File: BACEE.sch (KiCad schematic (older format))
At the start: 0 parts

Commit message: Create new shild sheet, added roject symbols
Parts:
- added BT?: Battery, symbol Device:Battery
- added C? (x2): C, symbol Device:C
- added C?: CP, symbol Device:CP
- added D?: LED, symbol Device:LED
- added R? (x2): R, symbol Device:R
- added U?: 24LC1025, symbol Memory_EEPROM:24LC1025
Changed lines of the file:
@@
 $Descr A4 11693 8268
 encoding utf-8
-Sheet 1 1
+Sheet 1 2
 Title "Battery Powered Arduino with clock and extended eeprom"
 Date "2020-05-17"
@@
 Comment4 ""
 $EndDescr
+$Comp
+L Device:Battery BT?
+U 1 1 5EC0DCA7
+P 5050 3050
+F 0 "BT?" H 5158 3096 50  0000 L CNN
+F 1 "Battery" H 5158 3005 50  0000 L CNN
+F 2 "" V 5050 3110 50  0001 C CNN
+F 3 "~" V 5050 3110 50  0001 C CNN
+	1    5050 3050
+	1    0    0    -1
+$EndComp
+$Comp
+L Device:C C?
+U 1 1 5EC0FEED
+P 5600 3000
+F 0 "C?" H 5715 3046 50  0000 L CNN
+F 1 "C" H 5715 2955 50  0000 L CNN
+F 2 "" H 5638 2850 50  0001 C CNN
+F 3 "~" H 5600 3000 50  0001 C CNN
+	1    5600 3000
+	1    0    0    -1
+$EndComp
+$Comp
+L Device:C C?
+U 1 1 5EC1064E
+P 5600 3500
+F 0 "C?" H 5715 3546 50  0000 L CNN
+F 1 "C" H 5715 3455 50  0000 L CNN
+F 2 "" H 5638 3350 50  0001 C CNN
+F 3 "~" H 5600 3500 50  0001 C CNN
+	1    5600 3500
+	1    0    0    -1
+$EndComp
+$Comp
+L Device:CP C?
+U 1 1 5EC10D42
+P 5600 4000
+F 0 "C?" H 5718 4046 50  0000 L CNN
+F 1 "CP" H 5718 3955 50  0000 L CNN
+F 2 "" H 5638 3850 50  0001 C CNN
+F 3 "~" H 5600 4000 50  0001 C CNN
+	1    5600 4000
+	1    0    0    -1
+$EndComp
+$Comp
+L Device:LED D?
+U 1 1 5EC11BF2
+P 5050 3750
+F 0 "D?" H 5043 3966 50  0000 C CNN
+F 1 "LED" H 5043 3875 50  0000 C CNN
+F 2 "" H 5050 3750 50  0001 C CNN
+F 3 "~" H 5050 3750 50  0001 C CNN
+	1    5050 3750
+	1    0    0    -1
+$EndComp
+$Comp
+L Device:R R?
+U 1 1 5EC1258B
+P 6300 3100
+F 0 "R?" H 6370 3146 50  0000 L CNN
+F 1 "R" H 6370 3055 50  0000 L CNN
+F 2 "" V 6230 3100 50  0001 C CNN
+F 3 "~" H 6300 3100 50  0001 C CNN
+	1    6300 3100
+	1    0    0    -1
+$EndComp
+$Comp
+L Device:R R?
+U 1 1 5EC1288A
+P 6300 3600
+F 0 "R?" H 6370 3646 50  0000 L CNN
+F 1 "R" H 6370 3555 50  0000 L CNN
+F 2 "" V 6230 3600 50  0001 C CNN
+F 3 "~" H 6300 3600 50  0001 C CNN
+	1    6300 3600
+	1    0    0    -1
+$EndComp
+$Comp
+L Memory_EEPROM:24LC1025 U?
+U 1 1 5EC12FEA
+P 7150 3050
+F 0 "U?" H 7150 3531 50  0000 C CNN
+F 1 "24LC1025" H 7150 3440 50  0000 C CNN
+F 2 "" H 7150 3050 50  0001 C CNN
+F 3 "http://ww1.microchip.com/downloads/en/DeviceDoc/21941B.pdf" H 7150 3050 50  0001 C CNN
+	1    7150 3050
+	1    0    0    -1
+$EndComp
+$Sheet
+S 6950 3850 1150 1600
+U 5EC178C4
+F0 "Connectors" 50
+F1 "Connectors.sch" 50
+$EndSheet
 $EndSCHEMATC

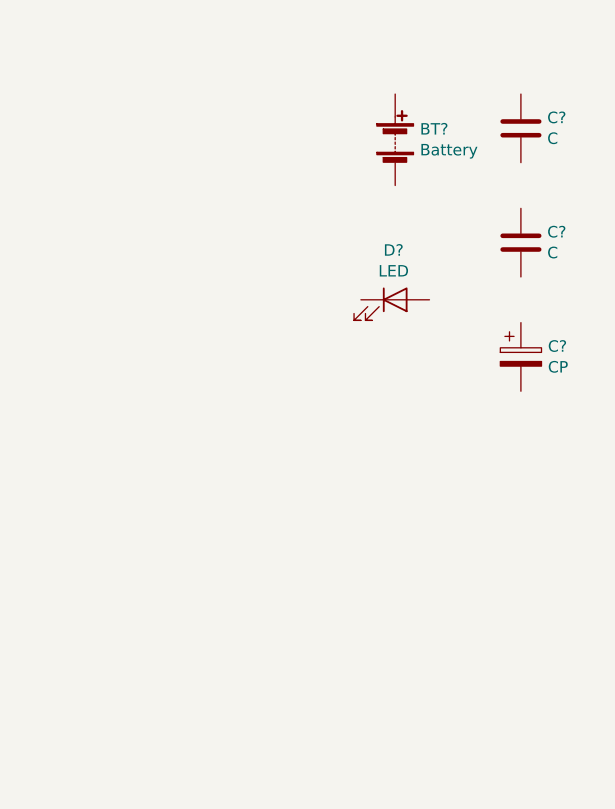
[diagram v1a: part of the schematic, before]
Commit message: Added symbol for Atmega328p-au
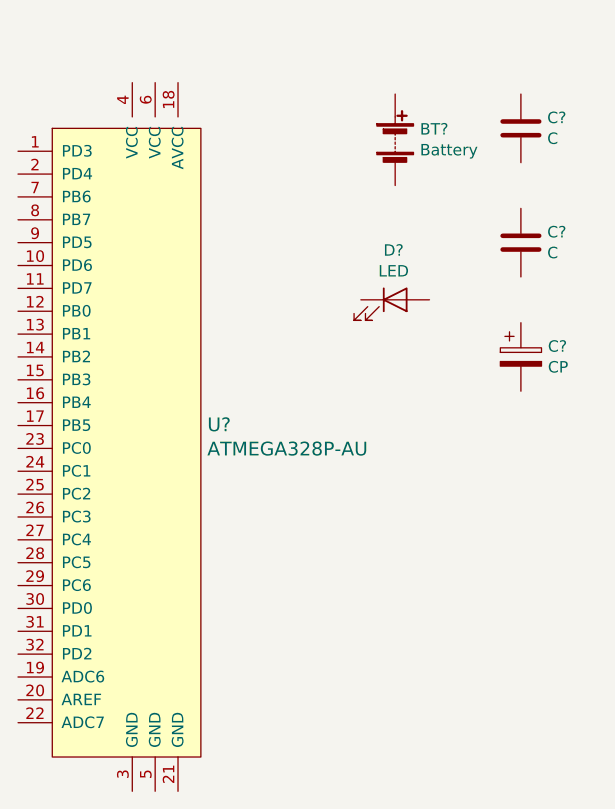
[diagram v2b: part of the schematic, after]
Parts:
- added U?: ATMEGA328P-AU, digikey-footprints:TQFP-32_7x7mm, symbol dk_Embedded-Microcontrollers:ATMEGA328P-AU
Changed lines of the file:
@@
 F1 "Connectors.sch" 50
 $EndSheet
+$Comp
+L dk_Embedded-Microcontrollers:ATMEGA328P-AU U?
+U 1 1 5EC1AF7B
+P 3900 4400
+F 0 "U?" H 4228 4503 60  0000 L CNN
+F 1 "ATMEGA328P-AU" H 4228 4397 60  0000 L CNN
+F 2 "digikey-footprints:TQFP-32_7x7mm" H 4100 4600 60  0001 L CNN
+F 3 "http://www.microchip.com/mymicrochip/filehandler.aspx?ddocname=en608326" H 4100 4700 60  0001 L CNN
+F 4 "ATMEGA328P-AU-ND" H 4100 4800 60  0001 L CNN "Digi-Key_PN"
+F 5 "ATMEGA328P-AU" H 4100 4900 60  0001 L CNN "MPN"
+F 6 "Integrated Circuits (ICs)" H 4100 5000 60  0001 L CNN "Category"
+F 7 "Embedded - Microcontrollers" H 4100 5100 60  0001 L CNN "Family"
+F 8 "http://www.microchip.com/mymicrochip/filehandler.aspx?ddocname=en608326" H 4100 5200 60  0001 L CNN "DK_Datasheet_Link"
+F 9 "/product-detail/en/microchip-technology/ATMEGA328P-AU/ATMEGA328P-AU-ND/1832260" H 4100 5300 60  0001 L CNN "DK_Detail_Page"
+F 10 "IC MCU 8BIT 32KB FLASH 32TQFP" H 4100 5400 60  0001 L CNN "Description"
+F 11 "Microchip Technology" H 4100 5500 60  0001 L CNN "Manufacturer"
+F 12 "Active" H 4100 5600 60  0001 L CNN "Status"
+	1    3900 4400
+	1    0    0    -1
+$EndComp
 $EndSCHEMATC

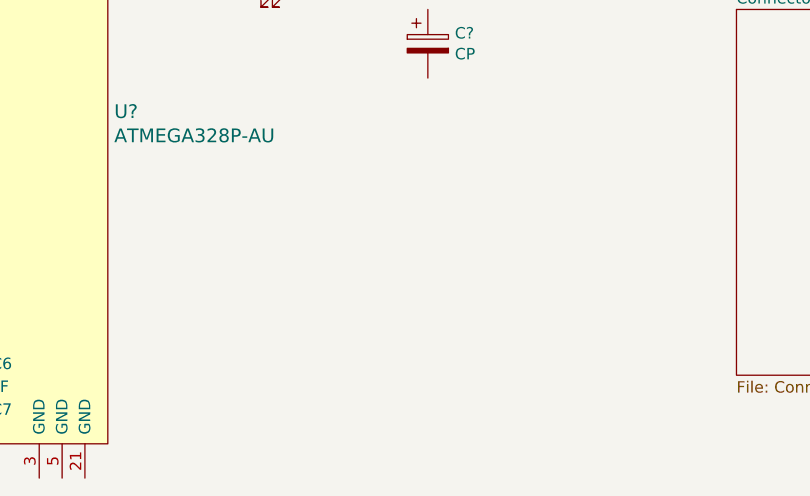
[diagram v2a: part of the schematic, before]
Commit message: Added clock IC Custom symbol
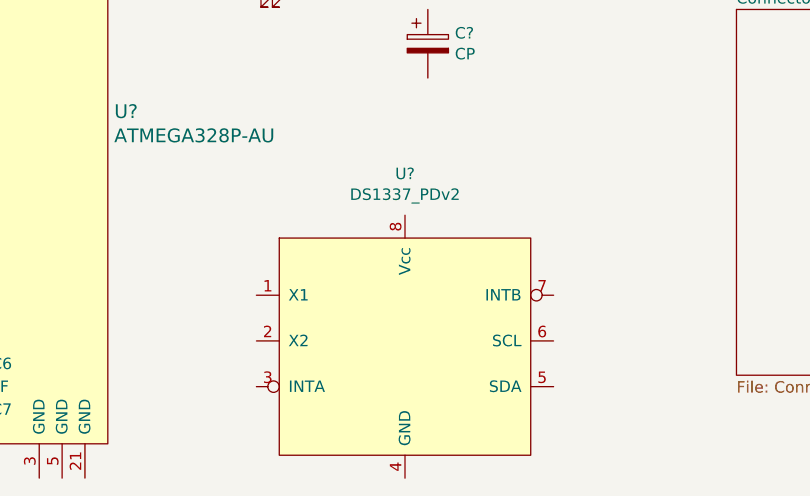
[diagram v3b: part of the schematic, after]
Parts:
- added U?: DS1337_PDv2, symbol Arduino-Library:DS1337_PDv2
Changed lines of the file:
@@
+	1    0    0    -1
+$EndComp
+$Comp
+L Arduino-Library:DS1337_PDv2 U?
+U 1 1 5EC1F02F
+P 5500 5300
+F 0 "U?" H 5500 6031 50  0000 C CNN
+F 1 "DS1337_PDv2" H 5500 5940 50  0000 C CNN
+F 2 "" H 6450 5800 50  0001 C CNN
+F 3 "https://4donline.ihs.com/images/VipMasterIC/IC/MAXM/MAXM-S-A0000633411/MAXM-S-A0000771822-1.pdf?hkey=52A5661711E402568146F3353EA87419" H 6450 5800 50  0001 C CNN
+	1    5500 5300
 	1    0    0    -1
 $EndComp

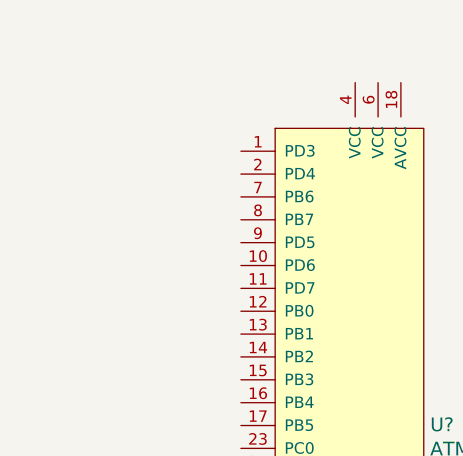
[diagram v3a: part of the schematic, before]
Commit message: Added crystals
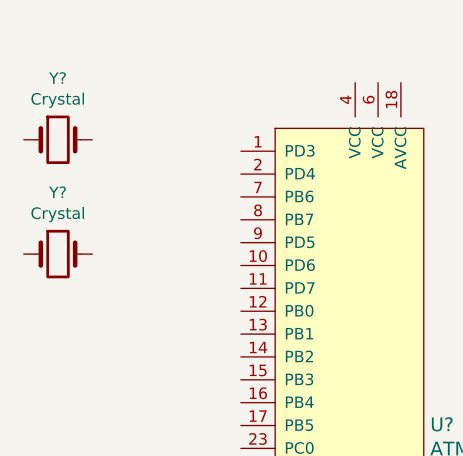
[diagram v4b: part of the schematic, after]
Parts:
- added Y? (x2): Crystal, symbol Device:Crystal
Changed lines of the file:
@@
+	1    0    0    -1
+$EndComp
+$Comp
+L Device:Crystal Y?
+U 1 1 5EC1F9D8
+P 2600 3050
+F 0 "Y?" H 2600 3318 50  0000 C CNN
+F 1 "Crystal" H 2600 3227 50  0000 C CNN
+F 2 "" H 2600 3050 50  0001 C CNN
+F 3 "~" H 2600 3050 50  0001 C CNN
+	1    2600 3050
+	1    0    0    -1
+$EndComp
+$Comp
+L Device:Crystal Y?
+U 1 1 5EC2101F
+P 2600 3550
+F 0 "Y?" H 2600 3818 50  0000 C CNN
+F 1 "Crystal" H 2600 3727 50  0000 C CNN
+F 2 "" H 2600 3550 50  0001 C CNN
+F 3 "~" H 2600 3550 50  0001 C CNN
+	1    2600 3550
 	1    0    0    -1
 $EndComp
